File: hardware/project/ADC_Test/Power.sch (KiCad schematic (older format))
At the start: 90 parts, among them U202 LM317_TO-263, U203 LM337_TO263, U204 LT8330_S6, U205 LM337_TO263, U301 TSR1-2490, U302 LM1117DTX-5.0/NOPB, U303 LT8330_S6, U304 LT8330_S6, U305 LT3030, U308 TSR1-2450, U309 LM1117DTX-3.3/NOPB

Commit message: Schematic design.
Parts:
- added C206: 10p, Capacitor_SMD:C_0603_1608Metric_Pad1.05x0.95mm_HandSolder, symbol Device:C
- added Q201: BC847W, Package_TO_SOT_SMD:SOT-323_SC-70, symbol Transistor_BJT:BC847W
- added R201: 10k, Resistor_SMD:R_0603_1608Metric_Pad1.05x0.95mm_HandSolder, symbol Device:R
- added R206: 1M, Resistor_SMD:R_0603_1608Metric_Pad1.05x0.95mm_HandSolder, symbol Device:R
- R213: renamed from R207; value R -> 1k6; footprint (none) -> Resistor_SMD:R_0603_1608Metric_Pad1.05x0.95mm_HandSolder
- R214: renamed from R208; footprint (none) -> Resistor_SMD:R_0603_1608Metric_Pad1.05x0.95mm_HandSolder
- R215: renamed from R209; value 1k2 -> 120; footprint (none) -> Resistor_SMD:R_0603_1608Metric_Pad1.05x0.95mm_HandSolder
- R216: renamed from R210; value 120 -> 240; footprint (none) -> Resistor_SMD:R_0603_1608Metric_Pad1.05x0.95mm_HandSolder
- R227: renamed from R215; footprint (none) -> Resistor_SMD:R_0603_1608Metric_Pad1.05x0.95mm_HandSolder
- R228: renamed from R216; value 120 -> 240; footprint (none) -> Resistor_SMD:R_0603_1608Metric_Pad1.05x0.95mm_HandSolder
- renumbered C304 to C201, C305 to C202, C307 to C203, C308 to C204, C301 to C205, C302 to C207, C310 to C208, C311 to C209, C312 to C210, C313 to C211, C303 to C212, C306 to C213, C309 to C214, C316 to C215, C317 to C216, C318 to C217, C319 to C218, C323 to C219, C324 to C220, C314 to C221, C315 to C222, C328 to C223, C329 to C224, C320 to C225, C321 to C226, C322 to C227, C223 to C228, C325 to C229, C224 to C230, C326 to C231, C327 to C232, C330 to C233, C331 to C234, C332 to C235, C225 to C236, C333 to C237, C334 to C238, C226 to C239, C335 to C240, C336 to C241, C337 to C242, C227 to C243, C228 to C244, C229 to C245, C230 to C246, D301 to D201, D302 to D202, D204 to D203, L301 to L201, L302 to L202, L303 to L203, L304 to L204, L201 to L205, R302 to R202, R303 to R203, R304 to R204, R305 to R205, R301 to R207, R307 to R208, R308 to R209, R309 to R210, R310 to R211, R306 to R212, R311 to R217, R312 to R218, R313 to R219, R314 to R220, R315 to R221, R316 to R222, R211 to R223, R212 to R224, R213 to R225, R214 to R226, U303 to U201, U304 to U202, U301 to U203, U302 to U204, U305 to U205, U202 to U206, U203 to U207, U308 to U208, U204 to U209, U309 to U210, U205 to U211
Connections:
- net labels added: FGPA_PWR_ON, GND, ~SHDN
- wire segments 363 -> 376

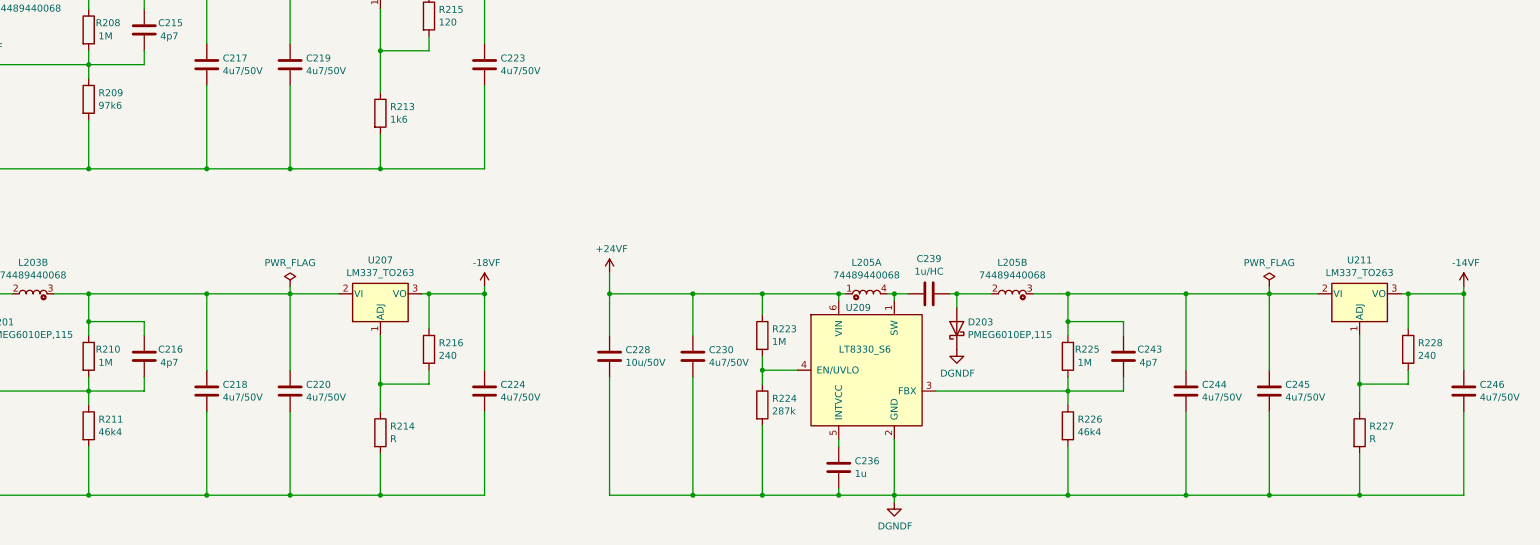
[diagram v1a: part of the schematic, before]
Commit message: Calculated voltages for the voltage sources.
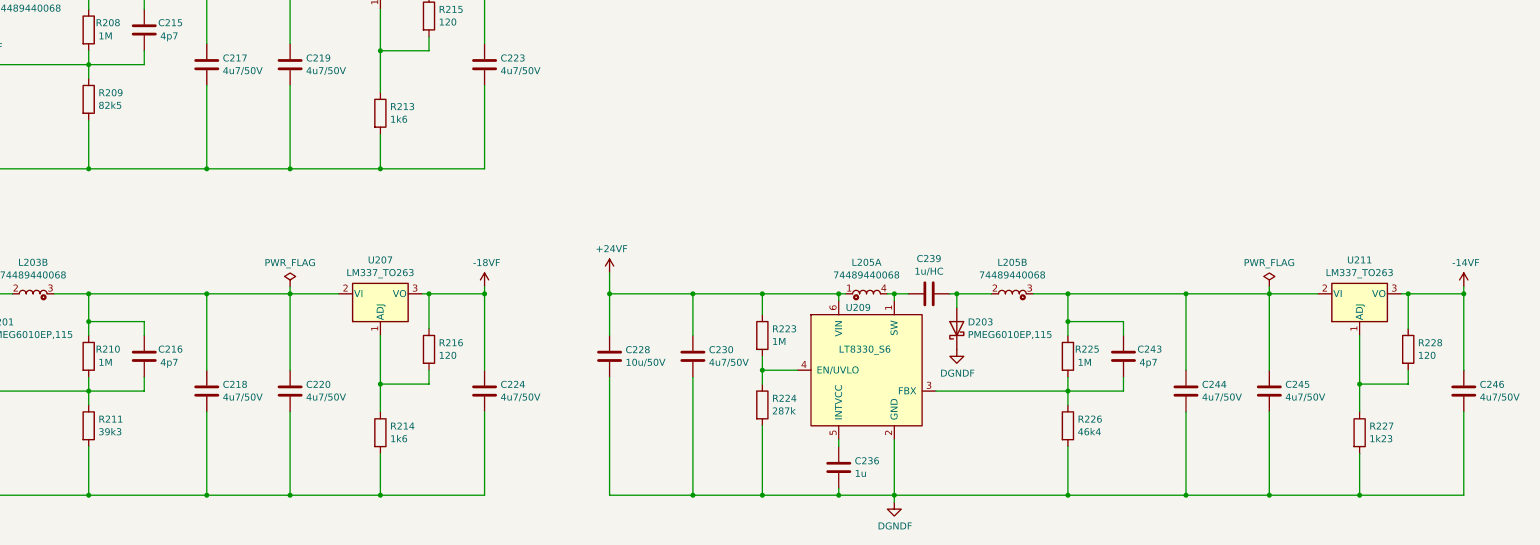
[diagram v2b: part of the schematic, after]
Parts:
- R209: value 97k6 -> 82k5
- R211: value 46k4 -> 39k3
- R214: value R -> 1k6
- R216, R228: value 240 -> 120
- R227: value R -> 1k23
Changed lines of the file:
@@
 P 4600 2500
 F 0 "R209" H 4670 2546 50  0000 L CNN
-F 1 "97k6" H 4670 2455 50  0000 L CNN
+F 1 "82k5" H 4670 2455 50  0000 L CNN
 F 2 "Resistor_SMD:R_0603_1608Metric_Pad1.05x0.95mm_HandSolder" V 4530 2500 50  0001 C CNN
 F 3 "~" H 4600 2500 50  0001 C CNN
@@
 P 4600 4850
 F 0 "R211" H 4670 4896 50  0000 L CNN
-F 1 "46k4" H 4670 4805 50  0000 L CNN
+F 1 "39k3" H 4670 4805 50  0000 L CNN
 F 2 "Resistor_SMD:R_0603_1608Metric_Pad1.05x0.95mm_HandSolder" V 4530 4850 50  0001 C CNN
 F 3 "~" H 4600 4850 50  0001 C CNN
@@
 P 6700 4900
 F 0 "R214" H 6770 4946 50  0000 L CNN
-F 1 "R" H 6770 4855 50  0000 L CNN
+F 1 "1k6" H 6770 4855 50  0000 L CNN
 F 2 "Resistor_SMD:R_0603_1608Metric_Pad1.05x0.95mm_HandSolder" V 6630 4900 50  0001 C CNN
 F 3 "~" H 6700 4900 50  0001 C CNN
@@
 P 7050 4300
 F 0 "R216" H 7120 4346 50  0000 L CNN
-F 1 "240" H 7120 4255 50  0000 L CNN
+F 1 "120" H 7120 4255 50  0000 L CNN
 F 2 "Resistor_SMD:R_0603_1608Metric_Pad1.05x0.95mm_HandSolder" V 6980 4300 50  0001 C CNN
 F 3 "~" H 7050 4300 50  0001 C CNN
@@
 P 13750 4900
 F 0 "R227" H 13820 4946 50  0000 L CNN
-F 1 "R" H 13820 4855 50  0000 L CNN
+F 1 "1k23" H 13820 4855 50  0000 L CNN
 F 2 "Resistor_SMD:R_0603_1608Metric_Pad1.05x0.95mm_HandSolder" V 13680 4900 50  0001 C CNN
 F 3 "~" H 13750 4900 50  0001 C CNN
@@
 P 14100 4300
 F 0 "R228" H 14170 4346 50  0000 L CNN
-F 1 "240" H 14170 4255 50  0000 L CNN
+F 1 "120" H 14170 4255 50  0000 L CNN
 F 2 "Resistor_SMD:R_0603_1608Metric_Pad1.05x0.95mm_HandSolder" V 14030 4300 50  0001 C CNN
 F 3 "~" H 14100 4300 50  0001 C CNN

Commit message: Schematic, PCB and BOM.
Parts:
- removed Q201: BC847W, Package_TO_SOT_SMD:SOT-323_SC-70, symbol Transistor_BJT:BC847W
- added Q201: BC847, Package_TO_SOT_SMD:SOT-23, symbol Transistor_BJT:BC847
- R211: value 39k3 -> 39k2
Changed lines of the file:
@@
 P 4600 4850
 F 0 "R211" H 4670 4896 50  0000 L CNN
-F 1 "39k3" H 4670 4805 50  0000 L CNN
+F 1 "39k2" H 4670 4805 50  0000 L CNN
 F 2 "Resistor_SMD:R_0603_1608Metric_Pad1.05x0.95mm_HandSolder" V 4530 4850 50  0001 C CNN
 F 3 "~" H 4600 4850 50  0001 C CNN
@@
 	3500 6650 3650 6650
 Connection ~ 3650 6650
-$Comp
-L Transistor_BJT:BC847W Q201
-U 1 1 5FCAF276
-P 2800 6950
-F 0 "Q201" H 2990 6996 50  0000 L CNN
-F 1 "BC847W" H 2990 6905 50  0000 L CNN
-F 2 "Package_TO_SOT_SMD:SOT-323_SC-70" H 3000 6875 50  0001 L CIN
-F 3 "http://www.infineon.com/dgdl/Infineon-BC847SERIES_BC848SERIES_BC849SERIES_BC850SERIES-DS-v01_01-en.pdf?fileId=db3a304314dca389011541d4630a1657" H 2800 6950 50  0001 L CNN
-	1    2800 6950
-	1    0    0    -1
-$EndComp
 Wire Wire Line
 	2900 6650 2900 6750
@@
 Wire Wire Line
 	11600 9350 11950 9350
+$Comp
+L Transistor_BJT:BC847 Q201
+U 1 1 5F8D0DAF
+P 2800 6950
+F 0 "Q201" H 2991 6996 50  0000 L CNN
+F 1 "BC847" H 2991 6905 50  0000 L CNN
+F 2 "Package_TO_SOT_SMD:SOT-23" H 3000 6875 50  0001 L CIN
+F 3 "http://www.infineon.com/dgdl/Infineon-BC847SERIES_BC848SERIES_BC849SERIES_BC850SERIES-DS-v01_01-en.pdf?fileId=db3a304314dca389011541d4630a1657" H 2800 6950 50  0001 L CNN
+	1    2800 6950
+	1    0    0    -1
+$EndComp
 $EndSCHEMATC

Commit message: PCB design
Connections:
- net +24VF: now also L203.1; no longer L202.3
- net AGNDF: now also L202.3; no longer L203.1
- net at C210.1, D202.2 (A): now also L202.2; no longer L203.4
- net at C211.2, U202.1 (SW): now also L203.4; no longer L202.2
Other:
- moved on the sheet: L202B, L203A
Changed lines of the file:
@@
 L ADC_TEST:74489440068 L203
 U 1 1 5DD443FC
-P 3850 1800
-F 0 "L203" V 3896 1728 50  0000 R CNN
-F 1 "74489440068" V 3805 1728 50  0000 R CNN
-F 2 "ADC_TEST:74489440068" H 3900 2200 50  0001 C CNN
-F 3 "" H 3900 2200 50  0001 C CNN
-	1    3850 1800
-	0    -1   -1   0
+P 3150 3900
+F 0 "L203" H 3250 4100 50  0000 R CNN
+F 1 "74489440068" H 3400 4000 50  0000 R CNN
+F 2 "ADC_TEST:74489440068" H 3200 4300 50  0001 C CNN
+F 3 "" H 3200 4300 50  0001 C CNN
+	1    3150 3900
+	1    0    0    -1
 $EndComp
 $Comp
@@
 L ADC_TEST:74489440068 L202
 U 2 1 5DE7207F
-P 3150 3900
-F 0 "L202" H 3150 4125 50  0000 C CNN
-F 1 "74489440068" H 3150 4034 50  0000 C CNN
-F 2 "ADC_TEST:74489440068" H 3200 4300 50  0001 C CNN
-F 3 "" H 3200 4300 50  0001 C CNN
-	2    3150 3900
-	1    0    0    -1
+P 3850 1800
+F 0 "L202" V 3900 1450 50  0000 C CNN
+F 1 "74489440068" V 3800 1450 50  0000 C CNN
+F 2 "ADC_TEST:74489440068" H 3900 2200 50  0001 C CNN
+F 3 "" H 3900 2200 50  0001 C CNN
+	2    3850 1800
+	0    -1   -1   0
 $EndComp
 Wire Wire Line
@@
 AR Path="/5E3DEC4F/5DED3D5A" Ref="U?"  Part="1"
 AR Path="/5FCAA619/5DED3D5A" Ref="U203"  Part="1"
+AR Path="/5DED3D5A" Ref="U?"  Part="1"
 F 0 "U203" H 3300 10065 50  0000 C CNN
 F 1 "TSR1-2490" H 3300 9974 50  0000 C CNN
@@
 AR Path="/5E3DEC4F/5E671CA2" Ref="U?"  Part="1"
 AR Path="/5FCAA619/5E671CA2" Ref="U208"  Part="1"
+AR Path="/5E671CA2" Ref="U?"  Part="1"
 F 0 "U208" H 9400 10065 50  0000 C CNN
 F 1 "TSR1-2450" H 9400 9974 50  0000 C CNN

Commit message: PCB design.
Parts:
- removed C206: 10p, Capacitor_SMD:C_0603_1608Metric_Pad1.05x0.95mm_HandSolder, symbol Device:C
- removed Q201: BC847, Package_TO_SOT_SMD:SOT-23, symbol Transistor_BJT:BC847
- removed R201: 10k, Resistor_SMD:R_0603_1608Metric_Pad1.05x0.95mm_HandSolder, symbol Device:R
- removed R206: 1M, Resistor_SMD:R_0603_1608Metric_Pad1.05x0.95mm_HandSolder, symbol Device:R
- renumbered C207 to C206, C208 to C207, C209 to C208, C210 to C209, C211 to C210, C212 to C211, C213 to C212, C214 to C213, C215 to C214, C216 to C215, C217 to C216, C218 to C217, C219 to C218, C220 to C219, C221 to C220, C222 to C221, C223 to C222, C224 to C223, C225 to C224, C226 to C225, C227 to C226, C228 to C227, C229 to C228, C230 to C229, C231 to C230, C232 to C231, C233 to C232, C234 to C233, C235 to C234, C236 to C235, C237 to C236, C238 to C237, C239 to C238, C240 to C239, C241 to C240, C242 to C241, C243 to C242, C244 to C243, C245 to C244, C246 to C245, R202 to R201, R203 to R202, R204 to R203, R205 to R204, R207 to R205, R208 to R206, R209 to R207, R210 to R208, R211 to R209, R212 to R210, R213 to R211, R214 to R212, R215 to R213, R216 to R214, R217 to R215, R218 to R216, R219 to R217, R220 to R218, R221 to R219, R222 to R220, R223 to R221, R224 to R222, R225 to R223, R226 to R224, R227 to R225, R228 to R226
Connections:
- net ~SHDN is gone; now on an unnamed net: U205.11 (~SHDN2), U205.20 (~SHDN1)
